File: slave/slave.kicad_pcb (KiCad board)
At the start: 2 copper layers, 235 x 10 mm, 10 parts

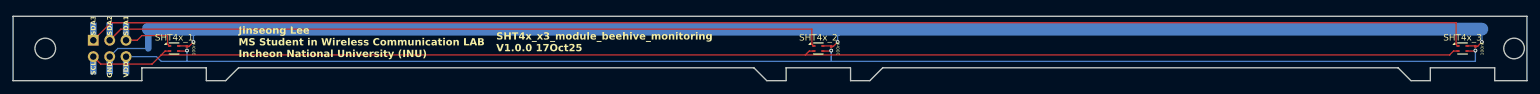
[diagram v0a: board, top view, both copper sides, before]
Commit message: udpate to v1.1.0
udpate to v1.1.0
master : modify connector 2.54->1.25
slave : modify capacitor 0201->0402
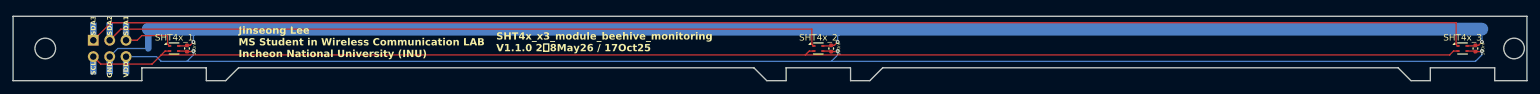
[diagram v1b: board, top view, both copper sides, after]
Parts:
- removed the 100nF at (152.0, 100.0)
- removed the 100nF at (252.0, 100.0)
- removed the 100nF at (52.0, 100.0)
- added 100nF: C_0402_1005Metric, Capacitor_SMD:C_0402_1005Metric, F.Cu at (252.0, 100.0)
- added 100nF: C_0402_1005Metric, Capacitor_SMD:C_0402_1005Metric, F.Cu at (152.0, 100.0)
- added 100nF: C_0402_1005Metric, Capacitor_SMD:C_0402_1005Metric, F.Cu at (52.0, 100.0)
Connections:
- REF** pad 3: (no net) -> vdd
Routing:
- net vdd: track 218.8 -> 223.2 mm
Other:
- board text added: "SHT4x_x3_module_beehive_monitoring V1.1.0 2묘8May26 / 17Oct25"
- board text removed: "SHT4x_x3_module_beehive_monitoring V1.0.0 17Oct25"
